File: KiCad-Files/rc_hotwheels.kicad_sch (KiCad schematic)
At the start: 14 parts, among them IC1 BD6211F-E2, IC2 MIC5504-3.3YM5-TR, U1 STM32F070F6P6, U3 NRF24L01_Breakout

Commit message: PCB V2.2
-Updated Capacitors footprint
-Added reset pin for the MCU.
-PCB design improved

Co-Authored-By: Yazid Almazroua <98489302+yazidta@users.noreply.github.com>
Co-Authored-By: Soplica52 <100694324+Soplica52@users.noreply.github.com>
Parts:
- C1, C4, C5, C6: footprint CAPC3225X105N -> C1uF:CAPC2012X135N
- C2: renamed from C7; footprint CAPC3225X105N -> C1uF:CAPC2012X135N
- C3: footprint CAPC3225X220N -> C1uF:CAPC2012X135N
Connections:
- net RST: now reaches U1.4 (NRST)
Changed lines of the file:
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@@
+    )
+  )
+  (global_label "RST" (shape input) (at 266.7 43.18 0) (fields_autoplaced)
+    (effects (font (size 1.27 1.27)) (justify left))
+    (property "Intersheetrefs" "${INTERSHEET_REFS}" (at 273.1323 43.18 0)
+      (effects (font (size 1.27 1.27)) (justify left) hide)
+    )
+    (property "RST" "" (at 266.7 45.3708 0)
+      (effects (font (size 1.27 1.27)) (justify left))
     )
   )
@@
       (effects (font (size 1.27 1.27)) (justify right))
     )
-    (property "Footprint" "CAPC3225X105N" (at -22.53 54.61 0)
+    (property "Footprint" "C1uF:CAPC2012X135N" (at -22.53 54.61 0)
       (effects (font (size 1.27 1.27)) (justify left top) hide)
     )
@@
       (effects (font (size 1.27 1.27)) (justify right))
     )
-    (property "Footprint" "CAPC3225X105N" (at 176.2 27.94 0)
+    (property "Footprint" "C1uF:CAPC2012X135N" (at 176.2 27.94 0)
       (effects (font (size 1.27 1.27)) (justify left top) hide)
     )
@@
       (effects (font (size 1.27 1.27)) (justify right))
     )
-    (property "Footprint" "CAPC3225X105N" (at 176.2 54.61 0)
+    (property "Footprint" "C1uF:CAPC2012X135N" (at 176.2 54.61 0)
       (effects (font (size 1.27 1.27)) (justify left top) hide)
     )
@@
       (effects (font (size 1.27 1.27)) (justify right))
     )
-    (property "Footprint" "CAPC3225X220N" (at -22.53 27.94 0)
+    (property "Footprint" "C1uF:CAPC2012X135N" (at -22.53 27.94 0)
       (effects (font (size 1.27 1.27)) (justify left top) hide)
     )
@@
   (symbol (lib_id "2023-11-22_23-54-19:STM32F070F6P6") (at 31.75 39.37 0) (unit 2)
     (in_bom yes) (on_board yes) (dnp no)
-    (property "Reference" "U1" (at 52.07 29.21 0)
+    (property "Reference" "U1" (at 59.69 29.21 0)
       (effects (font (size 1.524 1.524)))
     )
-    (property "Value" "STM32F070F6P6" (at 52.07 31.75 0)
+    (property "Value" "STM32F070F6P6" (at 59.69 31.75 0)
       (effects (font (size 1.524 1.524)))
     )
@@
   (symbol (lib_id "885012209003:885012209003") (at 73.66 102.87 270) (mirror x) (unit 1)
     (in_bom yes) (on_board yes) (dnp no)
-    (property "Reference" "C7" (at 69.85 95.25 90)
+    (property "Reference" "C2" (at 69.85 95.25 90)
       (effects (font (size 1.27 1.27)) (justify right))
     )
@@
       (effects (font (size 1.27 1.27)) (justify right))
     )
-    (property "Footprint" "CAPC3225X105N" (at -22.53 93.98 0)
+    (property "Footprint" "C1uF:CAPC2012X135N" (at -22.53 93.98 0)
       (effects (font (size 1.27 1.27)) (justify left top) hide)
     )
@@
       (project "rc_hotwheels"
         (path "/0b835094-f9c0-45ab-a312-d1f27d043c8e"
-          (reference "C7") (unit 1)
+          (reference "C2") (unit 1)
         )
       )
@@
       (effects (font (size 1.27 1.27)) (justify right))
     )
-    (property "Footprint" "CAPC3225X105N" (at -59.36 85.09 0)
-      (effects (font (size 1.27 1.27)) (justify left top) hide)
-    )
+    (property "Footprint" "C1uF:CAPC2012X135N" (at -59.36 85.09 0)
+      (effects (font (size 1.27 1.27)) (justify left top) hide)
+    )

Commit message: Files update
Bill of materials added
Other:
- company: (none) -> EA Bongo Bong - Konrad Marchewka Ahmed Bouras Yazid Almazroua
- title: (none) -> Remote Control Hotwheels
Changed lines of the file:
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@@
 (kicad_sch (version 20230121) (generator eeschema)
   (paper "A4")
+  (title_block
+    (title "Remote Control Hotwheels")
+    (date "2024-01-14")
+    (rev "v1.0")
+    (company "EA Bongo Bong - Konrad Marchewka Ahmed Bouras Yazid Almazroua")
+  )
   (junction (at 231.14 101.6) (diameter 0) (color 0 0 0 0)
   )

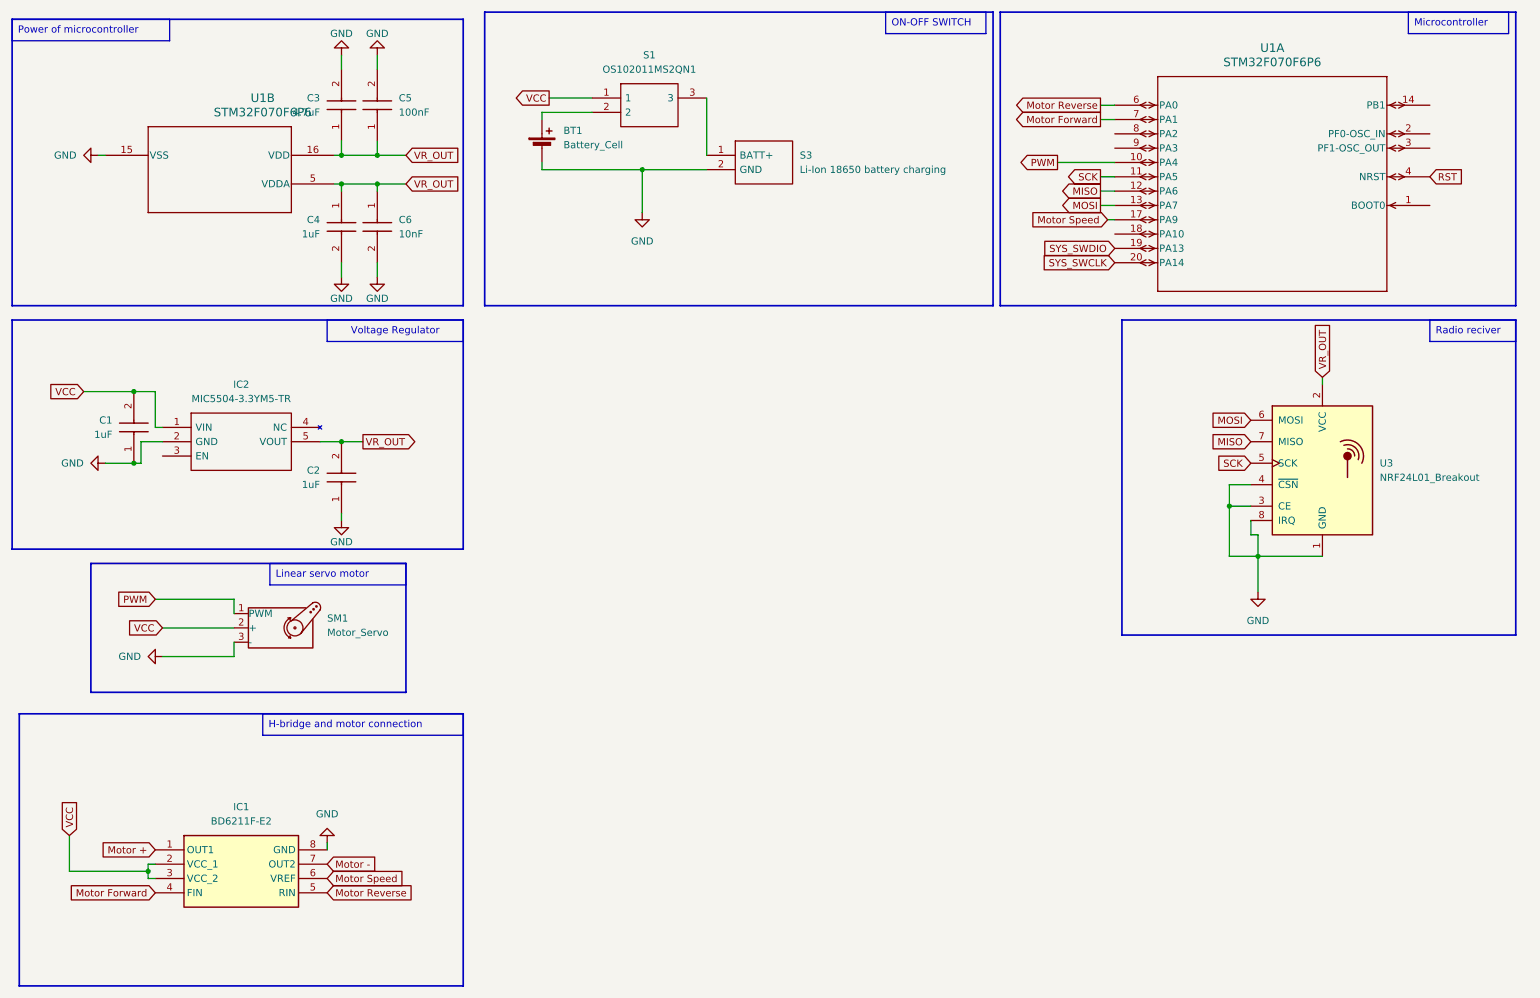
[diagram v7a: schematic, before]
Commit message: Changed Radio Receiver to Bluetooth Module
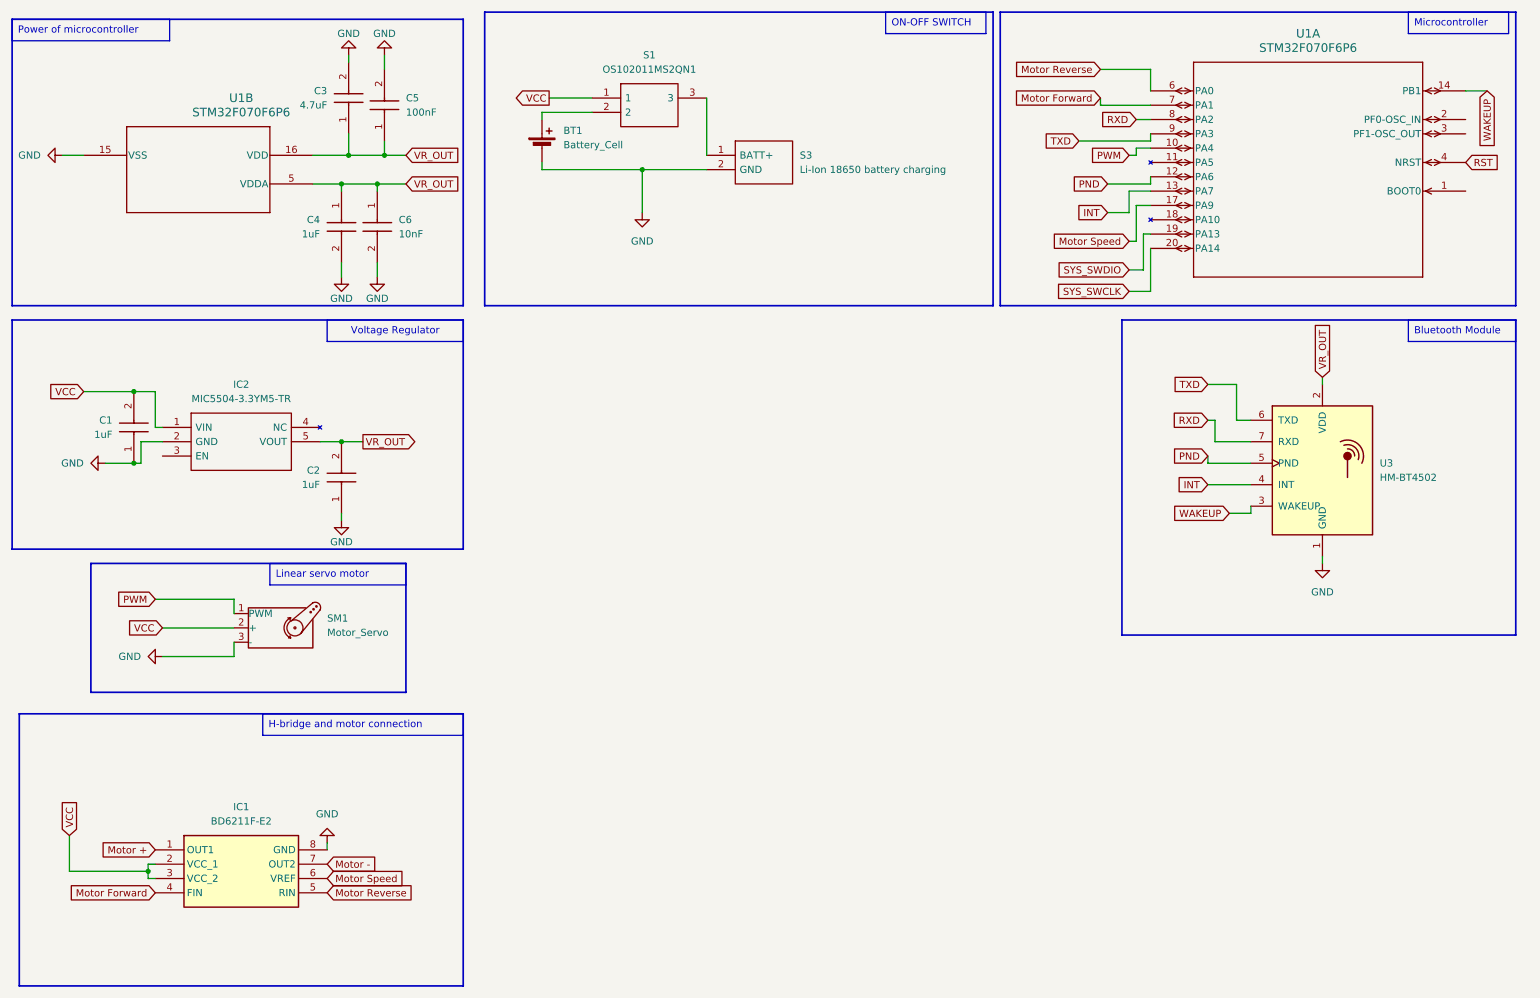
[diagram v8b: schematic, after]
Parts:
- U3: value NRF24L01_Breakout -> HM-BT4502
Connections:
- net WAKEUP: now reaches U1.14 (PB1)
- net WAKEUP: now also U3.3 (WAKEUP)
- net RXD: now reaches U1.8 (PA2)
- net RXD: now also U3.7 (RXD)
- net TXD: now reaches U1.9 (PA3)
- net TXD: now also U3.6 (TXD)
- net MISO renamed PND
- net PND: now also U3.5 (PND); no longer U3.7 (MISO)
- net MOSI renamed INT
- net INT: now also U3.4 (INT); no longer U3.6 (MOSI)
- net SCK: no longer names the net of U1.11 (PA5)
- net SCK: no longer U3.5 (SCK)
- now unconnected: U3.1 (GND)
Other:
- moved on the sheet: C3, C5, U1B
